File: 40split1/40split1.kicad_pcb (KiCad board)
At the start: 2 copper layers, 46 parts, among them U1 Raspberry_Pi_Pico, U2 TRRS

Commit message: adjusted pico position
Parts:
- moved U2 8.20 mm to (178.9, 77.0)
- moved U1 8.20 mm to (167.6, 45.7)
- moved D24 4.49 mm to (161.9, 82.5)
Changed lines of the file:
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@@
 	(footprint "ScottoKeebs_Components:TRRS_PJ-320A"
 		(layer "F.Cu")
-		(at 174.625 69.975 -90)
+		(at 178.865 76.995 -90)
 		(property "Reference" "U2"
 			(at 0 14.2 90)
@@
 	(footprint "ScottoKeebs_MCU:Raspberry_Pi_Pico"
 		(layer "F.Cu")
-		(at 163.4 38.7)
+		(at 167.64 45.72)
 		(property "Reference" "U1"
 			(at 0 -32 0)
@@
 	(footprint "ScottoKeebs_Components:Diode_DO-35"
 		(layer "F.Cu")
-		(at 165.1 79.375 150)
+		(at 161.925 82.55 150)
 		(descr "Diode, DO-35_SOD27 series, Axial, Horizontal, pin pitch=7.62mm, , length*diameter=4*2mm^2, , http://www.diodes.com/_files/packages/DO-35.pdf")
 		(tags "Diode DO-35_SOD27 series Axial Horizontal pin pitch 7.62mm  length 4mm diameter 2mm")

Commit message: adjusted schematics a little, finished all routing
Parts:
- moved D13 57.5 mm to (54.0, 76.2)
- moved D16 57.5 mm to (111.1, 69.8)
- moved D14 19.3 mm to (73.0, 73.0)
- moved D15 19.3 mm to (92.1, 69.8)
- moved U2 2.44 mm to (176.6, 76.2)
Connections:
- U1 pad 10: unconnected-(U1-GPIO7-Pad10) -> Row 1
- U1 pad 11: unconnected-(U1-GPIO8-Pad11) -> Row 2
- U1 pad 12: unconnected-(U1-GPIO9-Pad12) -> Row 3
- U1 pad 21: unconnected-(U1-GPIO16-Pad21) -> r2
- U1 pad 22: unconnected-(U1-GPIO17-Pad22) -> r1
- U1 pad 24: Row 3 -> unconnected-(U1-GPIO18-Pad24)
- U1 pad 25: Row 2 -> unconnected-(U1-GPIO19-Pad25)
- U1 pad 26: Row 1 -> unconnected-(U1-GPIO20-Pad26)
- U1 pad 27: Row 0 -> unconnected-(U1-GPIO21-Pad27)
- U1 pad 5: r1 -> unconnected-(U1-GPIO3-Pad5)
- U1 pad 6: r2 -> unconnected-(U1-GPIO4-Pad6)
- U1 pad 9: unconnected-(U1-GPIO6-Pad9) -> Row 0
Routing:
- net Col 0: track 0.00 -> 190.6 mm
- net Col 2: track 0.00 -> 174.9 mm
- net Col 1: track 0.00 -> 170.6 mm
- net Col 3: track 0.00 -> 158.1 mm
- net Col 4: track 0.00 -> 144.5 mm
- net Col 5: track 0.00 -> 136.2 mm
- net Row 2: track 0.00 -> 125.6 mm
- net Row 3: track 0.00 -> 115.7 mm
- net Row 0: track 0.00 -> 112.9 mm
- net Row 1: track 0.00 -> 110.0 mm
- net Tip: track 0.00 -> 68.0 mm
- net r1: track 0.00 -> 13.7 mm
- net r2: track 0.00 -> 10.4 mm
- net Net-(D23-A): track 0.00 -> 9.11 mm
- net Net-(D24-A): track 0.00 -> 8.73 mm
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
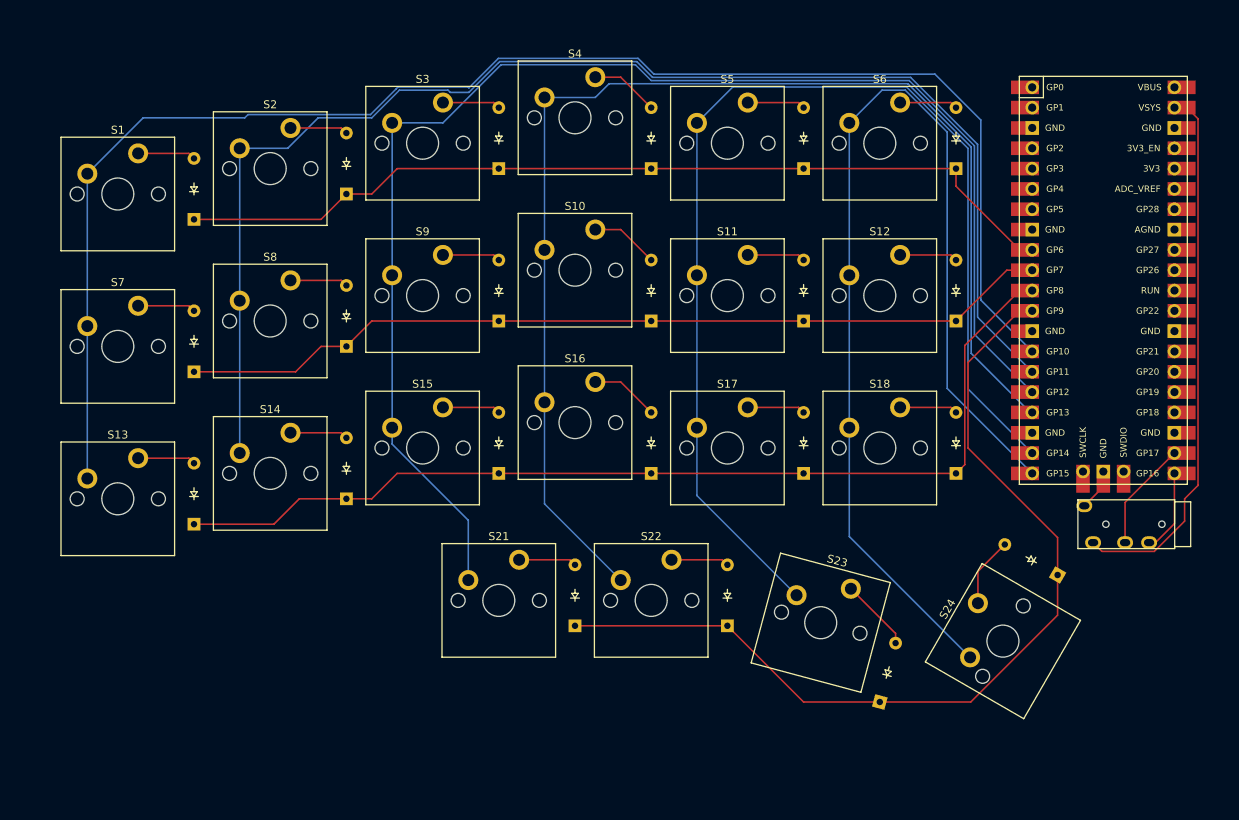
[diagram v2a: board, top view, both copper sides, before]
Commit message: did the pcb cutout, flipped all the diodes
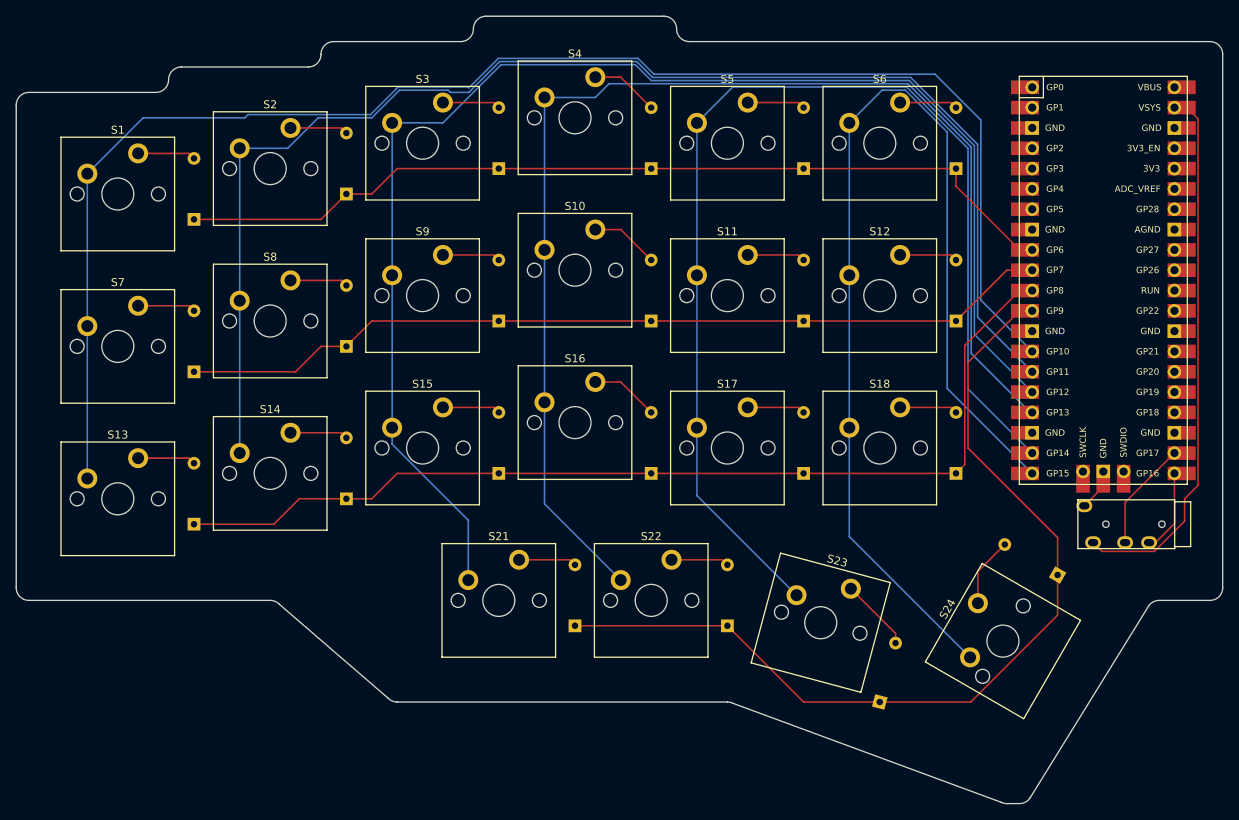
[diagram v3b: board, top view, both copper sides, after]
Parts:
- D1, D10, D11, D12, D13, D14, D15, D16, D17, D18, D2, D21, D22, D23, D24, D3, D4, D5, D6, D7, D8, D9: moved to B.Cu
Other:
- board outline added: 150.8 x 98.4 mm
